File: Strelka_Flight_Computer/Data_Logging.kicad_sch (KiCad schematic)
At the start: 7 parts, among them IC1 XTSD04GLGEAG

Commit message: Changed design rules
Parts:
- IC1: footprint SON127P800X600X95-8N -> Footprints:SON127P800X600X95-8N
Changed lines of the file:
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@@
       (effects (font (size 1.27 1.27)))
     )
-    (property "Footprint" "SON127P800X600X95-8N" (at 104.775 48.26 0)
+    (property "Footprint" "Footprints:SON127P800X600X95-8N" (at 104.775 48.26 0)
       (effects (font (size 1.27 1.27)) (justify left) hide)
     )

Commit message: Routing starting
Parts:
- removed R36, R37, R38, R39: 47k, Resistor_SMD:R_0603_1608Metric, symbol Device:R_Small
- added R20, R23, R24, R25: 47k, Resistor_SMD:R_0402_1005Metric, symbol Device:R_Small
- C31: footprint Capacitor_SMD:C_0603_1608Metric -> Capacitor_SMD:C_0402_1005Metric
- R35: footprint Resistor_SMD:R_0603_1608Metric -> Resistor_SMD:R_0402_1005Metric; LCSC (none) -> C25792
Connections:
- net +3V3: now also R20.1, R23.1, R24.1, R25.1
- net SD0: now also R25.2
- net SD1: now also R24.2
- net SD2: now also R23.2
- net SD3: now also R20.2
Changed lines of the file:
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@@
     (effects (font (size 1.27 1.27)) (justify right))
   )
+  (symbol (lib_id "Device:R_Small") (at 68.58 79.375 0) (unit 1)
+    (in_bom yes) (on_board yes) (dnp no) (fields_autoplaced)
+    (property "Reference" "R25" (at 70.0787 78.4665 0)
+      (effects (font (size 1.27 1.27)) (justify left))
+    )
+    (property "Value" "47k" (at 70.0787 81.2416 0)
+      (effects (font (size 1.27 1.27)) (justify left))
+    )
+    (property "Footprint" "Resistor_SMD:R_0402_1005Metric" (at 68.58 79.375 0)
+      (effects (font (size 1.27 1.27)) hide)
+    )
+    (property "Datasheet" "~" (at 68.58 79.375 0)
+      (effects (font (size 1.27 1.27)) hide)
+    )
+    (property "LCSC" "C25792" (at 68.58 79.375 0)
+      (effects (font (size 1.27 1.27)) hide)
+    )
+    (pin "1")
+    (pin "2")
+    (instances
+      (project "Strelka_Flight_Computer"
+        (path "/e63e39d7-6ac0-4ffd-8aa3-1841a4541b55/e94c6cea-6c6c-4b5f-a840-b97a15d9406a"
+          (reference "R25") (unit 1)
+        )
+      )
+    )
+  )
   (symbol (lib_id "power:+3.3V") (at 110.49 33.655 0) (unit 1)
     (in_bom yes) (on_board yes) (dnp no) (fields_autoplaced)
@@
         (path "/e63e39d7-6ac0-4ffd-8aa3-1841a4541b55/e94c6cea-6c6c-4b5f-a840-b97a15d9406a"
           (reference "#PWR0171") (unit 1)
-        )
-      )
-    )
-  )
-  (symbol (lib_id "Device:R_Small") (at 62.23 79.375 0) (unit 1)
-    (in_bom yes) (on_board yes) (dnp no) (fields_autoplaced)
-    (property "Reference" "R38" (at 63.7287 78.4665 0)
-      (effects (font (size 1.27 1.27)) (justify left))
-    )
-    (property "Value" "47k" (at 63.7287 81.2416 0)
-      (effects (font (size 1.27 1.27)) (justify left))
-    )
-    (property "Footprint" "Resistor_SMD:R_0603_1608Metric" (at 62.23 79.375 0)
-      (effects (font (size 1.27 1.27)) hide)
-    )
-    (property "Datasheet" "~" (at 62.23 79.375 0)
-      (effects (font (size 1.27 1.27)) hide)
-    )
-    (pin "1")
-    (pin "2")
-    (instances
-      (project "Strelka_Flight_Computer"
-        (path "/e63e39d7-6ac0-4ffd-8aa3-1841a4541b55/e94c6cea-6c6c-4b5f-a840-b97a15d9406a"
-          (reference "R38") (unit 1)
         )
       )
@@
       (effects (font (size 1.27 1.27)) (justify left))
     )
-    (property "Footprint" "Capacitor_SMD:C_0603_1608Metric" (at 110.49 36.195 0)
+    (property "Footprint" "Capacitor_SMD:C_0402_1005Metric" (at 110.49 36.195 0)
       (effects (font (size 1.27 1.27)) hide)
     )
@@
       (effects (font (size 1.27 1.27)) (justify left))
     )
-    (property "Footprint" "Resistor_SMD:R_0603_1608Metric" (at 42.545 79.375 0)
+    (property "Footprint" "Resistor_SMD:R_0402_1005Metric" (at 42.545 79.375 0)
       (effects (font (size 1.27 1.27)) hide)
     )
@@
       (effects (font (size 1.27 1.27)) hide)
     )
+    (property "LCSC" "C25792" (at 42.545 79.375 0)
+      (effects (font (size 1.27 1.27)) hide)
+    )
     (pin "1")
     (pin "2")
@@
     )
   )
+  (symbol (lib_id "Device:R_Small") (at 48.895 79.375 0) (unit 1)
+    (in_bom yes) (on_board yes) (dnp no) (fields_autoplaced)
+    (property "Reference" "R20" (at 50.3937 78.4665 0)
+      (effects (font (size 1.27 1.27)) (justify left))
+    )
+    (property "Value" "47k" (at 50.3937 81.2416 0)
+      (effects (font (size 1.27 1.27)) (justify left))
+    )
+    (property "Footprint" "Resistor_SMD:R_0402_1005Metric" (at 48.895 79.375 0)
+      (effects (font (size 1.27 1.27)) hide)
+    )
+    (property "Datasheet" "~" (at 48.895 79.375 0)
+      (effects (font (size 1.27 1.27)) hide)
+    )
+    (property "LCSC" "C25792" (at 48.895 79.375 0)
+      (effects (font (size 1.27 1.27)) hide)
+    )
+    (pin "1")
+    (pin "2")
+    (instances
+      (project "Strelka_Flight_Computer"
+        (path "/e63e39d7-6ac0-4ffd-8aa3-1841a4541b55/e94c6cea-6c6c-4b5f-a840-b97a15d9406a"
+          (reference "R20") (unit 1)
+        )
+      )
+    )
+  )
   (symbol (lib_id "power:+3.3V") (at 97.155 39.37 0) (unit 1)
     (in_bom yes) (on_board yes) (dnp no) (fields_autoplaced)
@@
         (path "/e63e39d7-6ac0-4ffd-8aa3-1841a4541b55/e94c6cea-6c6c-4b5f-a840-b97a15d9406a"
           (reference "#PWR0170") (unit 1)
-        )
-      )
-    )
-  )
-  (symbol (lib_id "Device:R_Small") (at 55.245 79.375 0) (unit 1)
-    (in_bom yes) (on_board yes) (dnp no) (fields_autoplaced)
-    (property "Reference" "R37" (at 56.7437 78.4665 0)
-      (effects (font (size 1.27 1.27)) (justify left))
-    )
-    (property "Value" "47k" (at 56.7437 81.2416 0)
-      (effects (font (size 1.27 1.27)) (justify left))
-    )
-    (property "Footprint" "Resistor_SMD:R_0603_1608Metric" (at 55.245 79.375 0)
-      (effects (font (size 1.27 1.27)) hide)
-    )
-    (property "Datasheet" "~" (at 55.245 79.375 0)
-      (effects (font (size 1.27 1.27)) hide)
-    )
-    (pin "1")
-    (pin "2")
-    (instances
-      (project "Strelka_Flight_Computer"
-        (path "/e63e39d7-6ac0-4ffd-8aa3-1841a4541b55/e94c6cea-6c6c-4b5f-a840-b97a15d9406a"
-          (reference "R37") (unit 1)
-        )
-      )
-    )
-  )
-  (symbol (lib_id "Device:R_Small") (at 48.895 79.375 0) (unit 1)
-    (in_bom yes) (on_board yes) (dnp no) (fields_autoplaced)
-    (property "Reference" "R36" (at 50.3937 78.4665 0)
-      (effects (font (size 1.27 1.27)) (justify left))
-    )
-    (property "Value" "47k" (at 50.3937 81.2416 0)
-      (effects (font (size 1.27 1.27)) (justify left))
-    )
-    (property "Footprint" "Resistor_SMD:R_0603_1608Metric" (at 48.895 79.375 0)
-      (effects (font (size 1.27 1.27)) hide)
-    )
-    (property "Datasheet" "~" (at 48.895 79.375 0)
-      (effects (font (size 1.27 1.27)) hide)
-    )
-    (pin "1")
-    (pin "2")
-    (instances
-      (project "Strelka_Flight_Computer"
-        (path "/e63e39d7-6ac0-4ffd-8aa3-1841a4541b55/e94c6cea-6c6c-4b5f-a840-b97a15d9406a"
-          (reference "R36") (unit 1)
-        )
-      )
-    )
-  )
-  (symbol (lib_id "Device:R_Small") (at 68.58 79.375 0) (unit 1)
-    (in_bom yes) (on_board yes) (dnp no) (fields_autoplaced)
-    (property "Reference" "R39" (at 70.0787 78.4665 0)
-      (effects (font (size 1.27 1.27)) (justify left))
-    )
-    (property "Value" "47k" (at 70.0787 81.2416 0)
-      (effects (font (size 1.27 1.27)) (justify left))
-    )
-    (property "Footprint" "Resistor_SMD:R_0603_1608Metric" (at 68.58 79.375 0)
-      (effects (font (size 1.27 1.27)) hide)
-    )
-    (property "Datasheet" "~" (at 68.58 79.375 0)
-      (effects (font (size 1.27 1.27)) hide)
-    )
-    (pin "1")
-    (pin "2")
-    (instances
-      (project "Strelka_Flight_Computer"
-        (path "/e63e39d7-6ac0-4ffd-8aa3-1841a4541b55/e94c6cea-6c6c-4b5f-a840-b97a15d9406a"
-          (reference "R39") (unit 1)
         )
       )
@@
         (path "/e63e39d7-6ac0-4ffd-8aa3-1841a4541b55/e94c6cea-6c6c-4b5f-a840-b97a15d9406a"
           (reference "#PWR0195") (unit 1)
+        )
+      )
+    )
+  )
+  (symbol (lib_id "Device:R_Small") (at 55.245 79.375 0) (unit 1)
+    (in_bom yes) (on_board yes) (dnp no) (fields_autoplaced)
+    (property "Reference" "R23" (at 56.7437 78.4665 0)
+      (effects (font (size 1.27 1.27)) (justify left))
+    )
+    (property "Value" "47k" (at 56.7437 81.2416 0)
+      (effects (font (size 1.27 1.27)) (justify left))
+    )
+    (property "Footprint" "Resistor_SMD:R_0402_1005Metric" (at 55.245 79.375 0)
+      (effects (font (size 1.27 1.27)) hide)
+    )
+    (property "Datasheet" "~" (at 55.245 79.375 0)
+      (effects (font (size 1.27 1.27)) hide)
+    )
+    (property "LCSC" "C25792" (at 55.245 79.375 0)
+      (effects (font (size 1.27 1.27)) hide)
+    )
+    (pin "1")
+    (pin "2")
+    (instances
+      (project "Strelka_Flight_Computer"
+        (path "/e63e39d7-6ac0-4ffd-8aa3-1841a4541b55/e94c6cea-6c6c-4b5f-a840-b97a15d9406a"
+          (reference "R23") (unit 1)
         )
       )
@@
         )
       )
+    )
+  )
+  (symbol (lib_id "Device:R_Small") (at 62.23 79.375 0) (unit 1)
+    (in_bom yes) (on_board yes) (dnp no) (fields_autoplaced)
+    (property "Reference" "R24" (at 63.7287 78.4665 0)
+      (effects (font (size 1.27 1.27)) (justify left))
+    )
+    (property "Value" "47k" (at 63.7287 81.2416 0)
+      (effects (font (size 1.27 1.27)) (justify left))
+    )
+    (property "Footprint" "Resistor_SMD:R_0402_1005Metric" (at 62.23 79.375 0)
+      (effects (font (size 1.27 1.27)) hide)
+    )
+    (property "Datasheet" "~" (at 62.23 79.375 0)
+      (effects (font (size 1.27 1.27)) hide)
+    )
+    (property "LCSC" "C25792" (at 62.23 79.375 0)
+      (effects (font (size 1.27 1.27)) hide)
+    )
+    (pin "1")
+    (pin "2")
+    (instances
+      (project "Strelka_Flight_Computer"
+        (path "/e63e39d7-6ac0-4ffd-8aa3-1841a4541b55/e94c6cea-6c6c-4b5f-a840-b97a15d9406a"
+          (reference "R24") (unit 1)
+        )
+      )

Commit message: Continued routing
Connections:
- net +3V3 renamed +3.3V
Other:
- note removed: "Double check these pins"
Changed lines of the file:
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@@
     (effects (font (size 3.9878 3.9878)) (justify left bottom))
-  )
-  (text "Double check these pins" (at 119.38 23.495 0)
-    (effects (font (size 1.27 1.27)) (justify left bottom))
   )
   (hierarchical_label "CLK" (shape input) (at 41.275 53.34 180) (fields_autoplaced)
@@
     (effects (font (size 1.27 1.27)) (justify right))
   )
+  (symbol (lib_name "+3.3V_1") (lib_id "power:+3.3V") (at 110.49 33.655 0) (unit 1)
+    (in_bom yes) (on_board yes) (dnp no) (fields_autoplaced)
+    (property "Reference" "#PWR06" (at 110.49 37.465 0)
+      (effects (font (size 1.27 1.27)) hide)
+    )
+    (property "Value" "+3.3V" (at 110.49 30.48 0)
+      (effects (font (size 1.27 1.27)))
+    )
+    (property "Footprint" "" (at 110.49 33.655 0)
+      (effects (font (size 1.27 1.27)) hide)
+    )
+    (property "Datasheet" "" (at 110.49 33.655 0)
+      (effects (font (size 1.27 1.27)) hide)
+    )
+    (pin "1")
+    (instances
+      (project "Strelka_Flight_Computer"
+        (path "/e63e39d7-6ac0-4ffd-8aa3-1841a4541b55/e94c6cea-6c6c-4b5f-a840-b97a15d9406a"
+          (reference "#PWR06") (unit 1)
+        )
+      )
+    )
+  )
+  (symbol (lib_name "+3.3V_1") (lib_id "power:+3.3V") (at 55.245 75.565 0) (unit 1)
+    (in_bom yes) (on_board yes) (dnp no) (fields_autoplaced)
+    (property "Reference" "#PWR08" (at 55.245 79.375 0)
+      (effects (font (size 1.27 1.27)) hide)
+    )
+    (property "Value" "+3.3V" (at 55.245 72.39 0)
+      (effects (font (size 1.27 1.27)))
+    )
+    (property "Footprint" "" (at 55.245 75.565 0)
+      (effects (font (size 1.27 1.27)) hide)
+    )
+    (property "Datasheet" "" (at 55.245 75.565 0)
+      (effects (font (size 1.27 1.27)) hide)
+    )
+    (pin "1")
+    (instances
+      (project "Strelka_Flight_Computer"
+        (path "/e63e39d7-6ac0-4ffd-8aa3-1841a4541b55/e94c6cea-6c6c-4b5f-a840-b97a15d9406a"
+          (reference "#PWR08") (unit 1)
+        )
+      )
+    )
+  )
   (symbol (lib_id "Device:R_Small") (at 68.58 79.375 0) (unit 1)
     (in_bom yes) (on_board yes) (dnp no) (fields_autoplaced)
@@
         (path "/e63e39d7-6ac0-4ffd-8aa3-1841a4541b55/e94c6cea-6c6c-4b5f-a840-b97a15d9406a"
           (reference "R25") (unit 1)
-        )
-      )
-    )
-  )
-  (symbol (lib_id "power:+3.3V") (at 110.49 33.655 0) (unit 1)
-    (in_bom yes) (on_board yes) (dnp no) (fields_autoplaced)
-    (property "Reference" "#PWR0171" (at 110.49 37.465 0)
-      (effects (font (size 1.27 1.27)) hide)
-    )
-    (property "Value" "+3.3V" (at 110.49 30.0792 0)
-      (effects (font (size 1.27 1.27)))
-    )
-    (property "Footprint" "" (at 110.49 33.655 0)
-      (effects (font (size 1.27 1.27)) hide)
-    )
-    (property "Datasheet" "" (at 110.49 33.655 0)
-      (effects (font (size 1.27 1.27)) hide)
-    )
-    (pin "1")
-    (instances
-      (project "Strelka_Flight_Computer"
-        (path "/e63e39d7-6ac0-4ffd-8aa3-1841a4541b55/e94c6cea-6c6c-4b5f-a840-b97a15d9406a"
-          (reference "#PWR0171") (unit 1)
         )
       )
@@
     )
   )
-  (symbol (lib_id "power:+3.3V") (at 97.155 39.37 0) (unit 1)
-    (in_bom yes) (on_board yes) (dnp no) (fields_autoplaced)
-    (property "Reference" "#PWR0170" (at 97.155 43.18 0)
-      (effects (font (size 1.27 1.27)) hide)
-    )
-    (property "Value" "+3.3V" (at 97.155 35.7942 0)
-      (effects (font (size 1.27 1.27)))
-    )
-    (property "Footprint" "" (at 97.155 39.37 0)
-      (effects (font (size 1.27 1.27)) hide)
-    )
-    (property "Datasheet" "" (at 97.155 39.37 0)
-      (effects (font (size 1.27 1.27)) hide)
-    )
-    (pin "1")
-    (instances
-      (project "Strelka_Flight_Computer"
-        (path "/e63e39d7-6ac0-4ffd-8aa3-1841a4541b55/e94c6cea-6c6c-4b5f-a840-b97a15d9406a"
-          (reference "#PWR0170") (unit 1)
-        )
-      )
-    )
-  )
   (symbol (lib_id "power:GND") (at 110.49 38.735 0) (unit 1)
     (in_bom yes) (on_board yes) (dnp no)
@@
         (path "/e63e39d7-6ac0-4ffd-8aa3-1841a4541b55/e94c6cea-6c6c-4b5f-a840-b97a15d9406a"
           (reference "#PWR0195") (unit 1)
+        )
+      )
+    )
+  )
+  (symbol (lib_name "+3.3V_1") (lib_id "power:+3.3V") (at 97.155 39.37 0) (unit 1)
+    (in_bom yes) (on_board yes) (dnp no) (fields_autoplaced)
+    (property "Reference" "#PWR07" (at 97.155 43.18 0)
+      (effects (font (size 1.27 1.27)) hide)
+    )
+    (property "Value" "+3.3V" (at 97.155 36.195 0)
+      (effects (font (size 1.27 1.27)))
+    )
+    (property "Footprint" "" (at 97.155 39.37 0)
+      (effects (font (size 1.27 1.27)) hide)
+    )
+    (property "Datasheet" "" (at 97.155 39.37 0)
+      (effects (font (size 1.27 1.27)) hide)
+    )
+    (pin "1")
+    (instances
+      (project "Strelka_Flight_Computer"
+        (path "/e63e39d7-6ac0-4ffd-8aa3-1841a4541b55/e94c6cea-6c6c-4b5f-a840-b97a15d9406a"
+          (reference "#PWR07") (unit 1)
         )
       )
@@
         )
       )
-    )
-  )
-  (symbol (lib_id "power:+3.3V") (at 55.245 75.565 0) (unit 1)
-    (in_bom yes) (on_board yes) (dnp no) (fields_autoplaced)
-    (property "Reference" "#PWR0169" (at 55.245 79.375 0)
-      (effects (font (size 1.27 1.27)) hide)
-    )
-    (property "Value" "+3.3V" (at 55.245 71.9892 0)
-      (effects (font (size 1.27 1.27)))
-    )
-    (property "Footprint" "" (at 55.245 75.565 0)
-      (effects (font (size 1.27 1.27)) hide)
-    )
-    (property "Datasheet" "" (at 55.245 75.565 0)
-      (effects (font (size 1.27 1.27)) hide)
-    )
-    (pin "1")
-    (instances
-      (project "Strelka_Flight_Computer"
-        (path "/e63e39d7-6ac0-4ffd-8aa3-1841a4541b55/e94c6cea-6c6c-4b5f-a840-b97a15d9406a"
-          (reference "#PWR0169") (unit 1)
-        )
-      )

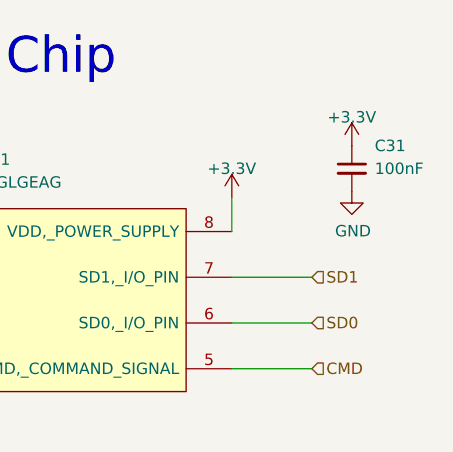
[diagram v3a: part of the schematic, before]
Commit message: Created BOM
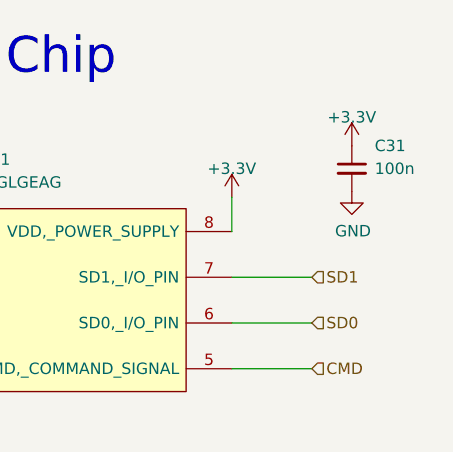
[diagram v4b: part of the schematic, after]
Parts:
- C31: value 100nF -> 100n
- IC1: LCSC (none) -> C558839; LCSC# C558839 -> (none)
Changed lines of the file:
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@@
       (effects (font (size 1.27 1.27)) (justify left))
     )
-    (property "Value" "100nF" (at 113.03 36.195 0)
+    (property "Value" "100n" (at 113.03 36.195 0)
       (effects (font (size 1.27 1.27)) (justify left))
     )
@@
       (effects (font (size 1.27 1.27)) (justify left) hide)
     )
-    (property "LCSC#" "C558839" (at 45.085 50.8 0)
+    (property "LCSC" "C558839" (at 45.085 50.8 0)
       (effects (font (size 1.27 1.27)) hide)
     )

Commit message: Added LCSC mpn to all relevent parts
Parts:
- C31: LCSC (none) -> C1525
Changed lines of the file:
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@@
+      (effects (font (size 1.27 1.27)) hide)
+    )
+    (property "LCSC" " C1525" (at 110.49 36.195 0)
       (effects (font (size 1.27 1.27)) hide)
     )
